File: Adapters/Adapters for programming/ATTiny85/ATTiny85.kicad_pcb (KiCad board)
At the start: 2 copper layers, 53.3 x 49.5 mm, 2 parts, among them U2 ATtiny85

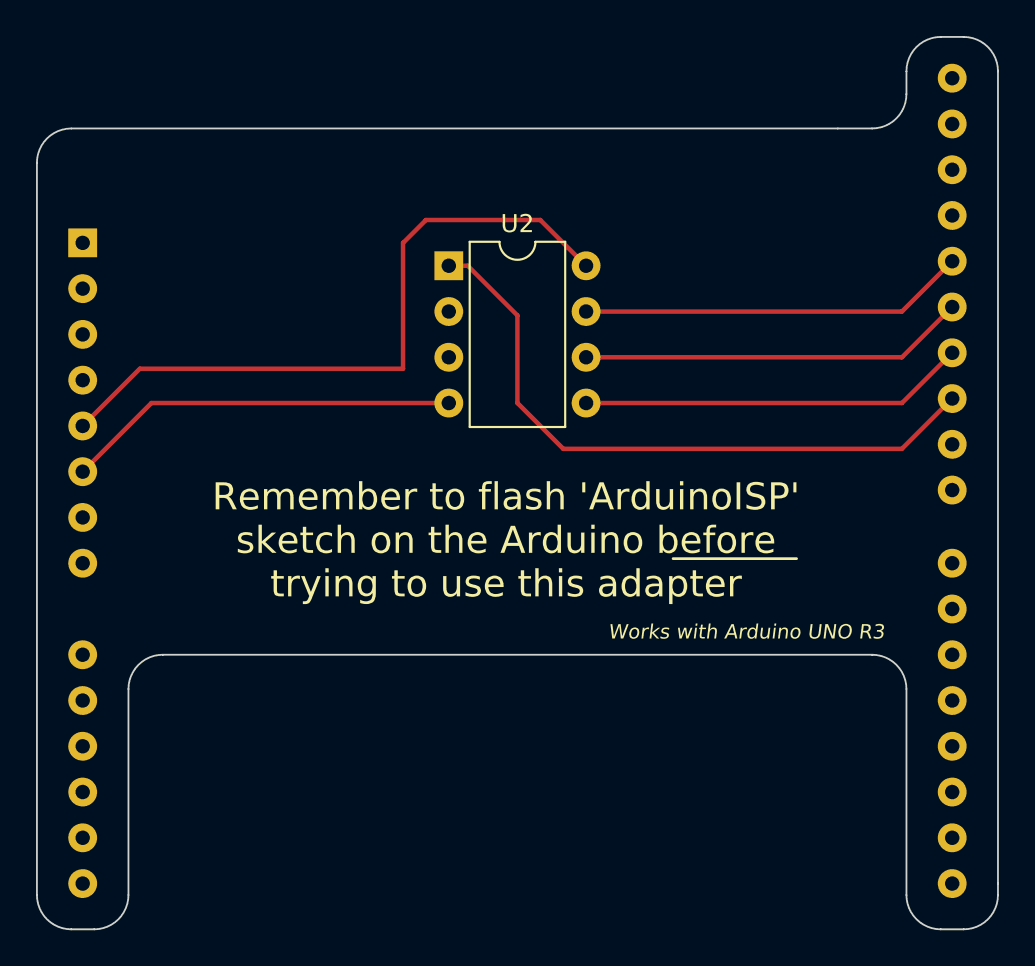
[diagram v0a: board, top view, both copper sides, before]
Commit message: Added Gerber files for Attiny85 adapter, fixed gitignore file
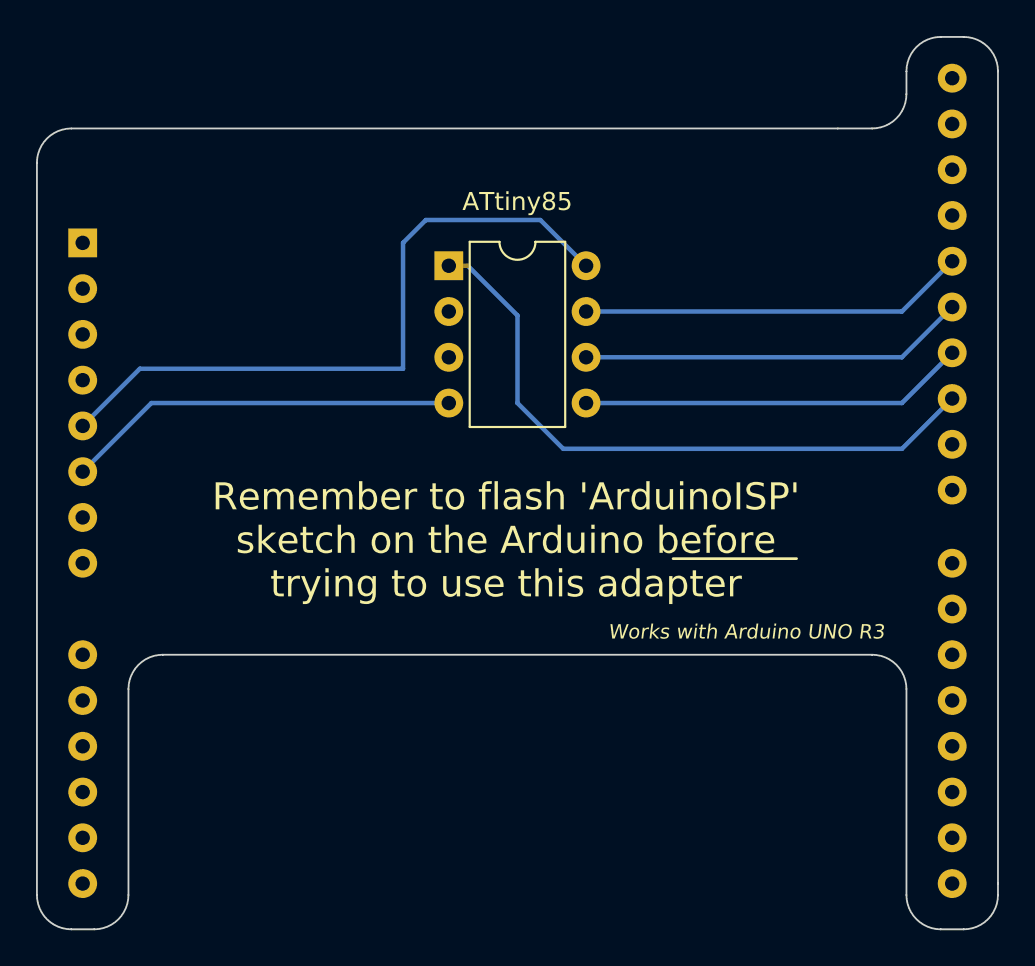
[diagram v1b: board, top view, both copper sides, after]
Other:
- board text added: "March 2020"
- board text added: "by Razvan"
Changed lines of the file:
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@@
   (general
     (thickness 1.6)
-    (drawings 25)
+    (drawings 28)
     (tracks 20)
     (zones 0)
@@
     (pad_to_mask_clearance 0)
     (aux_axis_origin 0 0)
-    (visible_elements 7FFFFFFF)
+    (visible_elements 7FFFFF7F)
     (pcbplotparams
       (layerselection 0x010fc_ffffffff)
@@
       (outputformat 1)
       (mirror false)
-      (drillshape 1)
+      (drillshape 0)
       (scaleselection 1)
-      (outputdirectory ""))
+      (outputdirectory "Gerber/"))
   )
   (net 0 "")
@@
     (uvia_dia 0.3)
     (uvia_drill 0.1)
-    (add_net "Net-(A1-Pad1)")
-    (add_net "Net-(A1-Pad10)")
-    (add_net "Net-(A1-Pad11)")
-    (add_net "Net-(A1-Pad12)")
-    (add_net "Net-(A1-Pad13)")
-    (add_net "Net-(A1-Pad14)")
-    (add_net "Net-(A1-Pad15)")
-    (add_net "Net-(A1-Pad16)")
-    (add_net "Net-(A1-Pad17)")
-    (add_net "Net-(A1-Pad18)")
-    (add_net "Net-(A1-Pad19)")
-    (add_net "Net-(A1-Pad2)")
-    (add_net "Net-(A1-Pad20)")
-    (add_net "Net-(A1-Pad21)")
-    (add_net "Net-(A1-Pad22)")
-    (add_net "Net-(A1-Pad23)")
-    (add_net "Net-(A1-Pad24)")
     (add_net "Net-(A1-Pad25)")
     (add_net "Net-(A1-Pad26)")
     (add_net "Net-(A1-Pad27)")
     (add_net "Net-(A1-Pad28)")
-    (add_net "Net-(A1-Pad29)")
-    (add_net "Net-(A1-Pad3)")
-    (add_net "Net-(A1-Pad30)")
-    (add_net "Net-(A1-Pad31)")
-    (add_net "Net-(A1-Pad32)")
-    (add_net "Net-(A1-Pad4)")
     (add_net "Net-(A1-Pad5)")
     (add_net "Net-(A1-Pad6)")
-    (add_net "Net-(A1-Pad7)")
-    (add_net "Net-(A1-Pad8)")
-    (add_net "Net-(A1-Pad9)")
-    (add_net "Net-(U2-Pad2)")
-    (add_net "Net-(U2-Pad3)")
   )
   (module ArduinoUnoMultiProgrammerAdapters:Arduino-UNO-R3-Shield (layer B.Cu)
@@
     (descr "8-lead though-hole mounted DIP package, row spacing 7.62 mm (300 mils)")
     (tags "THT DIP DIL PDIP 2.54mm 7.62mm 300mil")
-    (fp_text reference U2 (at 3.81 -2.33 180) (layer F.SilkS)
+    (fp_text reference U2 (at 3.81 -2.33 180) (layer F.SilkS) hide
       (effects (font (size 1 1) (thickness 0.15)))
     )
-    (fp_text value ATtiny85 (at 3.81 9.95 180) (layer F.Fab)
+    (fp_text value ATtiny85 (at 3.81 -3.556 180) (layer F.SilkS)
       (effects (font (size 1 1) (thickness 0.15)))
     )
@@
     )
   )
+  (gr_arc (start 161.29 125.476) (end 161.036 125.73) (angle -90) (layer B.SilkS) (width 0.15))
+  (gr_text "March 2020" (at 160.02 128.524) (layer B.SilkS)
+    (effects (font (size 1 1) (thickness 0.15)) (justify mirror))
+  )
+  (gr_text "by Razvan" (at 161.29 126.492) (layer B.SilkS)
+    (effects (font (size 1.5 1.5) (thickness 0.2)) (justify mirror))
+  )
   (gr_text "Works with Arduino UNO R3" (at 186.69 129.54) (layer F.SilkS)
     (effects (font (size 0.8 0.8) (thickness 0.15) italic))
@@
   (gr_arc (start 197.485 98.425) (end 197.485 96.52) (angle -90) (layer Edge.Cuts) (width 0.1))
   (gr_arc (start 198.755 98.425) (end 200.66 98.425) (angle -90) (layer Edge.Cuts) (width 0.1))
-  (segment (start 195.33 111.76) (end 198.12 108.97) (width 0.25) (layer F.Cu) (net 1))
-  (segment (start 177.8 111.76) (end 195.33 111.76) (width 0.25) (layer F.Cu) (net 1))
-  (segment (start 195.33 114.3) (end 198.12 111.51) (width 0.25) (layer F.Cu) (net 2))
-  (segment (start 177.8 114.3) (end 195.33 114.3) (width 0.25) (layer F.Cu) (net 2))
-  (segment (start 195.33 116.84) (end 198.12 114.05) (width 0.25) (layer F.Cu) (net 3))
-  (segment (start 177.8 116.84) (end 195.33 116.84) (width 0.25) (layer F.Cu) (net 3))
-  (segment (start 173.99 116.84) (end 176.53 119.38) (width 0.25) (layer F.Cu) (net 4))
-  (segment (start 195.33 119.38) (end 198.12 116.59) (width 0.25) (layer F.Cu) (net 4))
-  (segment (start 176.53 119.38) (end 195.33 119.38) (width 0.25) (layer F.Cu) (net 4))
+  (segment (start 195.33 111.76) (end 198.12 108.97) (width 0.25) (layer B.Cu) (net 1))
+  (segment (start 177.8 111.76) (end 195.33 111.76) (width 0.25) (layer B.Cu) (net 1))
+  (segment (start 195.33 114.3) (end 198.12 111.51) (width 0.25) (layer B.Cu) (net 2))
+  (segment (start 177.8 114.3) (end 195.33 114.3) (width 0.25) (layer B.Cu) (net 2))
+  (segment (start 195.33 116.84) (end 198.12 114.05) (width 0.25) (layer B.Cu) (net 3))
+  (segment (start 177.8 116.84) (end 195.33 116.84) (width 0.25) (layer B.Cu) (net 3))
+  (segment (start 173.99 116.84) (end 176.53 119.38) (width 0.25) (layer B.Cu) (net 4))
+  (segment (start 195.33 119.38) (end 198.12 116.59) (width 0.25) (layer B.Cu) (net 4))
+  (segment (start 176.53 119.38) (end 195.33 119.38) (width 0.25) (layer B.Cu) (net 4))
   (segment (start 171.23 109.22) (end 170.18 109.22) (width 0.25) (layer F.Cu) (net 4))
-  (segment (start 173.99 111.98) (end 171.23 109.22) (width 0.25) (layer F.Cu) (net 4))
-  (segment (start 173.99 116.84) (end 173.99 111.98) (width 0.25) (layer F.Cu) (net 4))
-  (segment (start 177.8 109.22) (end 175.26 106.68) (width 0.25) (layer F.Cu) (net 5))
-  (segment (start 175.26 106.68) (end 168.91 106.68) (width 0.25) (layer F.Cu) (net 5))
-  (segment (start 168.91 106.68) (end 167.64 107.95) (width 0.25) (layer F.Cu) (net 5))
-  (segment (start 167.64 107.95) (end 167.64 114.935) (width 0.25) (layer F.Cu) (net 5))
-  (segment (start 153.035 114.935) (end 149.86 118.11) (width 0.25) (layer F.Cu) (net 5))
-  (segment (start 167.64 114.935) (end 153.035 114.935) (width 0.25) (layer F.Cu) (net 5))
-  (segment (start 153.67 116.84) (end 149.86 120.65) (width 0.25) (layer F.Cu) (net 6))
-  (segment (start 170.18 116.84) (end 153.67 116.84) (width 0.25) (layer F.Cu) (net 6))
+  (segment (start 173.99 111.98) (end 171.23 109.22) (width 0.25) (layer B.Cu) (net 4))
+  (segment (start 173.99 116.84) (end 173.99 111.98) (width 0.25) (layer B.Cu) (net 4))
+  (segment (start 177.8 109.22) (end 175.26 106.68) (width 0.25) (layer B.Cu) (net 5))
+  (segment (start 175.26 106.68) (end 168.91 106.68) (width 0.25) (layer B.Cu) (net 5))
+  (segment (start 168.91 106.68) (end 167.64 107.95) (width 0.25) (layer B.Cu) (net 5))
+  (segment (start 167.64 107.95) (end 167.64 114.935) (width 0.25) (layer B.Cu) (net 5))
+  (segment (start 153.035 114.935) (end 149.86 118.11) (width 0.25) (layer B.Cu) (net 5))
+  (segment (start 167.64 114.935) (end 153.035 114.935) (width 0.25) (layer B.Cu) (net 5))
+  (segment (start 153.67 116.84) (end 149.86 120.65) (width 0.25) (layer B.Cu) (net 6))
+  (segment (start 170.18 116.84) (end 153.67 116.84) (width 0.25) (layer B.Cu) (net 6))
 )

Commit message: Signed all the boards, and re-generated the Gerber files
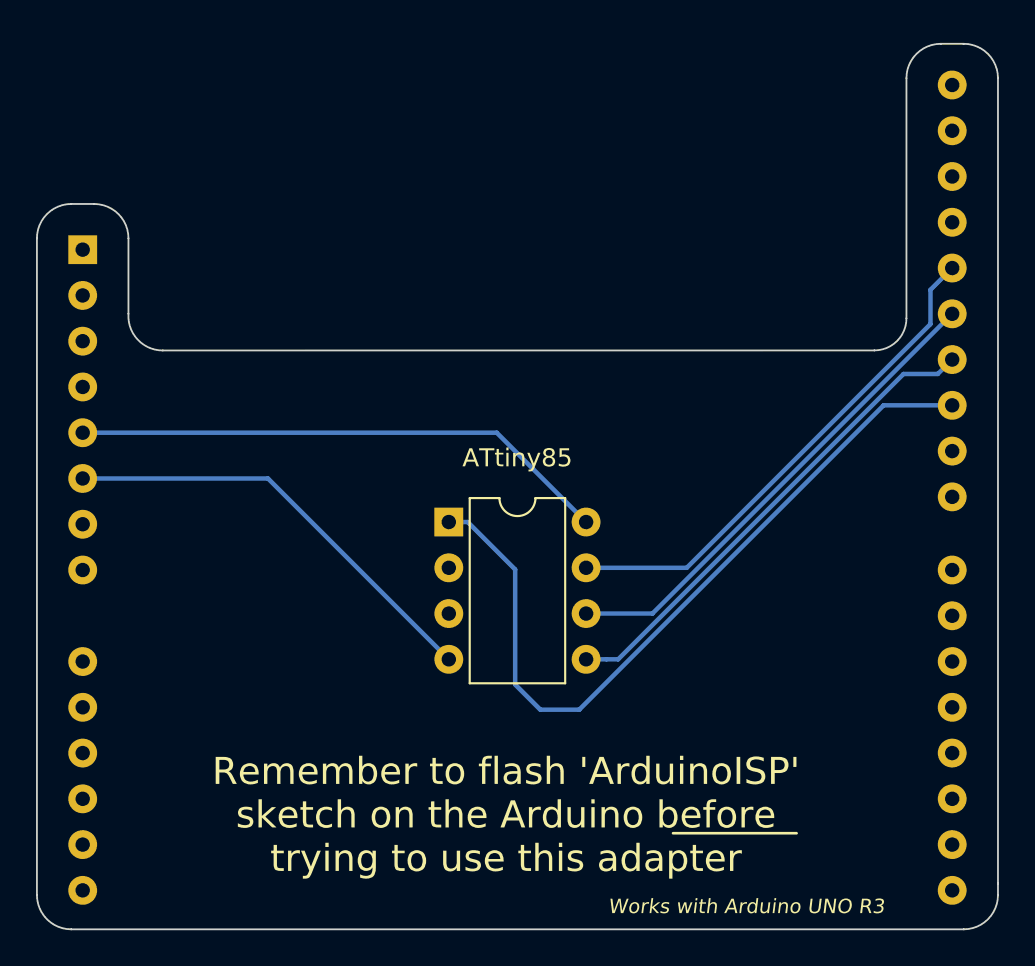
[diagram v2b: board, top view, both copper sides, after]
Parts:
- A1: footprint ArduinoUnoMultiProgrammerAdapters:Arduino-UNO-R3-Shield -> ArduinoUnoMultiProgrammerAdapters:Arduino_UNO_R3_Headers; moved to F.Cu
- moved A1 23.3 mm to (172.7, 112.8), turned to 0 degrees
- moved U2 14.2 mm to (170.2, 123.4)
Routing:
- net Net-(A1-Pad5): track 37.8 -> 30.0 mm
- net Net-(A1-Pad28): track 21.5 -> 28.3 mm
- net Net-(A1-Pad25): track 36.2 -> 43.0 mm
- net Net-(A1-Pad27): track 21.5 -> 27.2 mm
- net Net-(A1-Pad26): track 21.5 -> 27.2 mm
- net Net-(A1-Pad6): track 21.9 -> 24.5 mm
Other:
- board size 53.3 x 49.5 mm -> 53.3 x 49.1 mm
